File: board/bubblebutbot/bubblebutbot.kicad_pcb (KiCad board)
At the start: 2 copper layers, 80 x 86 mm, 15 parts, among them J1 Screw_Terminal_01x02, J2 Screw_Terminal_01x02, J3 Conn_01x06_Female, J4 Conn_01x06_Female, Q1 FDN336P, U1 WeMos_D1_mini, U2 18350-HOLDER, U3 TPS613222ADBV

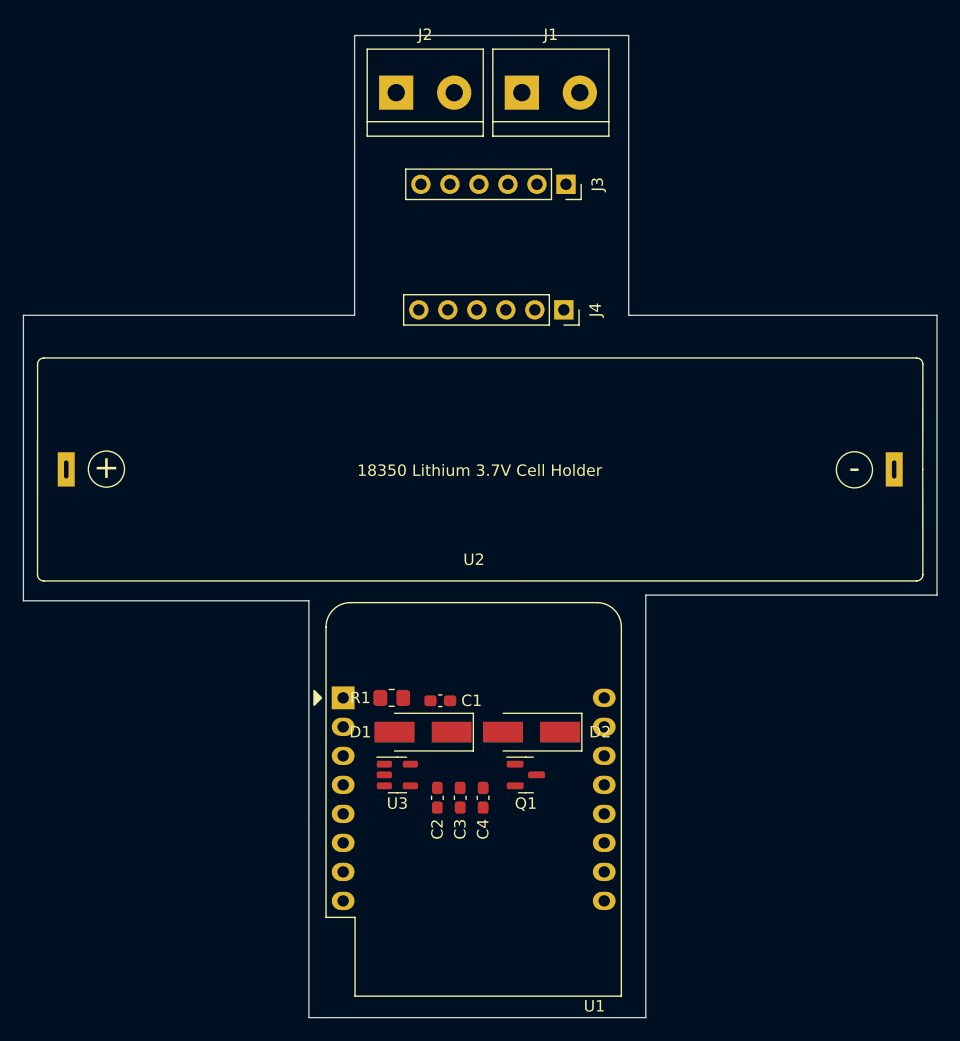
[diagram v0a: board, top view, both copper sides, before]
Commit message: Finished prototype pcb
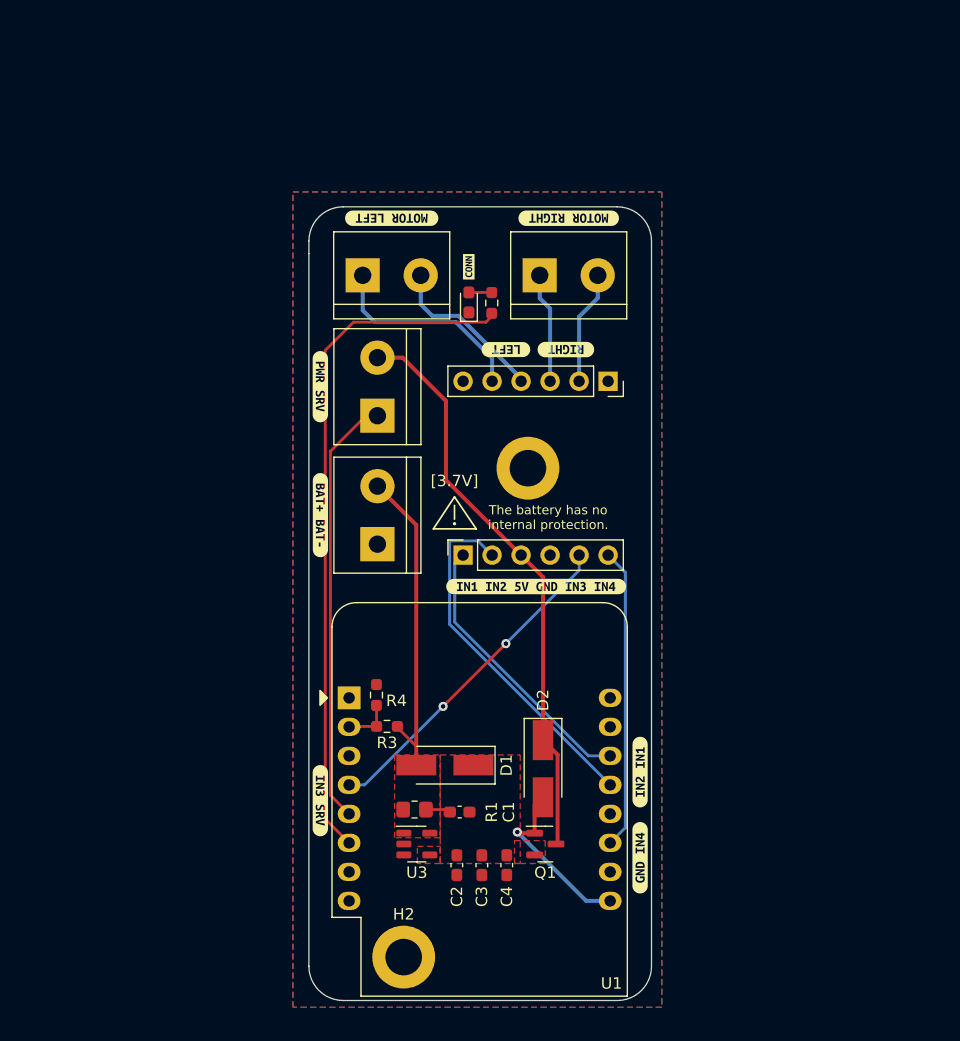
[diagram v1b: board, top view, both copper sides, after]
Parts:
- removed U2: 18350-HOLDER, CustomFootprints:18350-Holder
- added D3: LED, LED_SMD:LED_0603_1608Metric_Pad1.05x0.95mm_HandSolder, F.Cu at (165.0, 82.4)
- added H1: MountingHole, MountingHole:MountingHole_3.2mm_M3_ISO14580_Pad, F.Cu at (170.2, 96.9)
- added H2: MountingHole, MountingHole:MountingHole_3.2mm_M3_ISO14580_Pad, F.Cu at (159.3, 139.7)
- added J5: Screw_Terminal_01x02, TerminalBlock:TerminalBlock_bornier-2_P5.08mm, F.Cu at (157.0, 103.5)
- added J6: Screw_Terminal_01x02, TerminalBlock:TerminalBlock_bornier-2_P5.08mm, F.Cu at (157.0, 92.3)
- added R2: 1k, Resistor_SMD:R_0603_1608Metric_Pad0.98x0.95mm_HandSolder, F.Cu at (167.0, 82.4)
- added R3: 10k, Resistor_SMD:R_0603_1608Metric_Pad0.98x0.95mm_HandSolder, F.Cu at (157.8, 119.5)
- added R4: 33k, Resistor_SMD:R_0603_1608Metric_Pad0.98x0.95mm_HandSolder, F.Cu at (156.9, 116.8)
- added kibuzzard-641EE450: G***, kibuzzard-641EE450, F.Cu at (180.0, 123.5)
- added kibuzzard-641EE46F: G***, kibuzzard-641EE46F, F.Cu at (180.0, 131.0)
- added kibuzzard-641EE492: G***, kibuzzard-641EE492, F.Cu at (152.0, 126.0)
- added kibuzzard-641EE4C6: G***, kibuzzard-641EE4C6, F.Cu at (152.0, 101.0)
- added kibuzzard-641EE536: G***, kibuzzard-641EE536, F.Cu at (152.0, 89.8)
- added kibuzzard-641EE568: G***, kibuzzard-641EE568, F.Cu at (170.9, 107.2)
- added kibuzzard-641EE5F8: G***, kibuzzard-641EE5F8, F.Cu at (173.5, 86.5)
- added kibuzzard-641EE609: G***, kibuzzard-641EE609, F.Cu at (168.2, 86.5)
- added kibuzzard-641EE6B8: G***, kibuzzard-641EE6B8, F.Cu at (158.2, 75.0)
- added kibuzzard-641EE6C6: G***, kibuzzard-641EE6C6, F.Cu at (173.8, 75.0)
- added kibuzzard-641EE74D: G***, kibuzzard-641EE74D, F.Cu at (165.0, 79.2)
- moved J4 23.2 mm to (164.5, 104.5), turned to 90 degrees
- moved J3 17.6 mm to (177.2, 89.3)
- moved J2 16.3 mm to (155.7, 80.0)
- moved J1 16.1 mm to (171.2, 80.0)
- moved R1 9.98 mm to (160.2, 126.8)
- moved C1 9.90 mm to (164.2, 127.0)
- moved Q1 6.28 mm to (171.7, 129.8)
- moved U3 6.28 mm to (160.4, 129.8)
- moved C4 6.25 mm to (168.3, 131.7)
- moved C3 6.20 mm to (166.1, 131.7)
- moved C2 6.14 mm to (164.0, 131.7)
- moved D1 3.46 mm to (162.9, 122.9)
- moved D2 3.35 mm to (171.5, 123.2), turned to -90 degrees
- moved U1 0.52 mm to (154.5, 117.0)
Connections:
- U1 pad 2: unconnected-(U1-Pad2) -> BATTERY_LVL
- U1 pad 5: unconnected-(U1-Pad5) -> SERVO_PWM
- U1 pad 6: unconnected-(U1-Pad6) -> Net-(U1-Pad6)
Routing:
- net Net-(U1-Pad6): track 0.00 -> 60.2 mm
- net SPLY: track 0.00 -> 50.5 mm
- net SERVO_PWM: track 0.00 -> 37.8 mm
- net IN2: track 0.00 -> 31.4 mm
- net Net-(D1-Pad2): track 0.00 -> 30.0 mm
- net IN3: track 0.00 -> 29.3 mm, vias 0 -> 2
- net IN4: track 0.00 -> 26.4 mm
- net IN1: track 0.00 -> 24.6 mm
- net Net-(J2-Pad1): track 0.00 -> 17.9 mm
- net WEMOS_USB_POWER: track 0.00 -> 15.6 mm, vias 0 -> 1
- net Net-(J2-Pad2): track 0.00 -> 14.3 mm
- net Net-(J1-Pad2): track 0.00 -> 9.70 mm
- net Net-(J1-Pad1): track 0.00 -> 9.40 mm
- net BATTERY_LVL: track 0.00 -> 4.12 mm
- net Net-(C1-Pad1): track 0.00 -> 2.18 mm
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- added copper zone on B.Cu, net GND
- added copper zone on F.Cu, net GND
- added copper zone on F.Cu, net Net-(C1-Pad2)
- added copper zone on F.Cu, net Net-(D1-Pad2)
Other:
- board size 80 x 86 mm -> 30 x 69.5 mm
- board text added: "The battery has no internal protection."
- board text added: "[3.7V]"

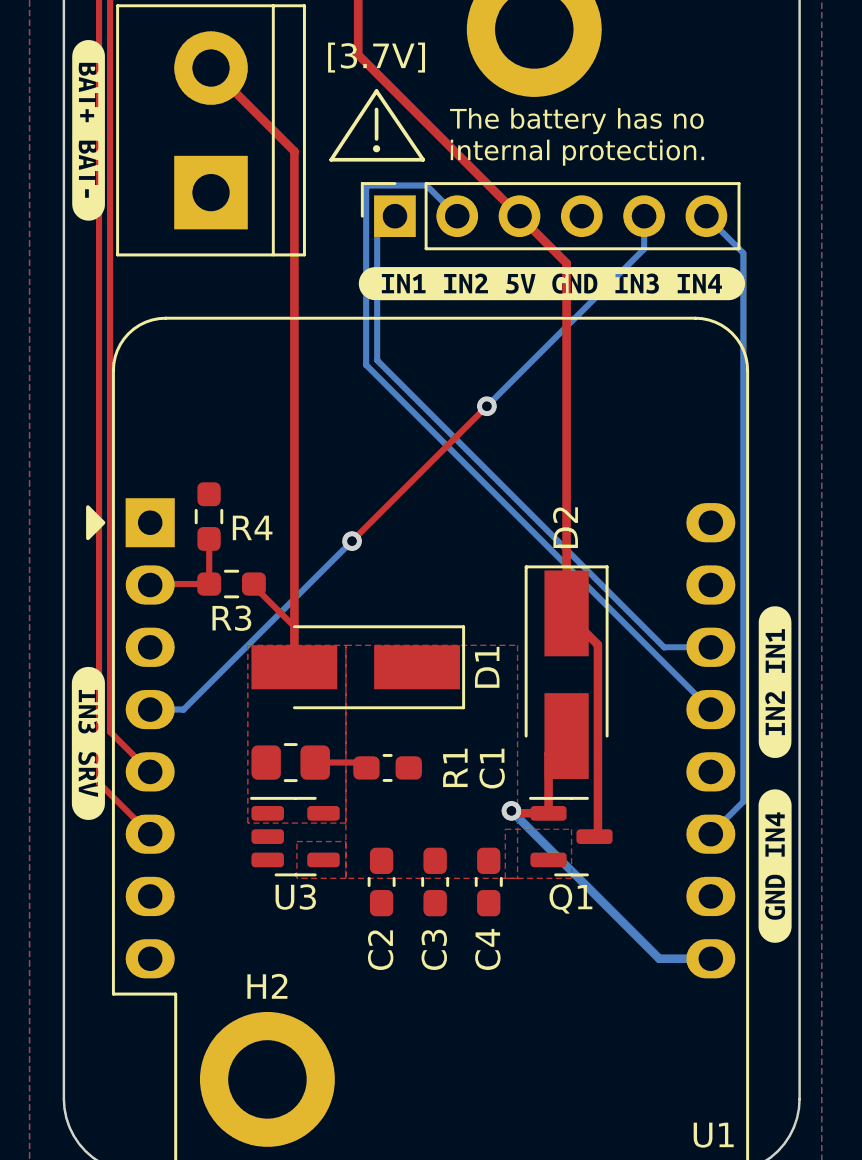
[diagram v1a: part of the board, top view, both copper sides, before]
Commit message: Added a missing inductor to the design
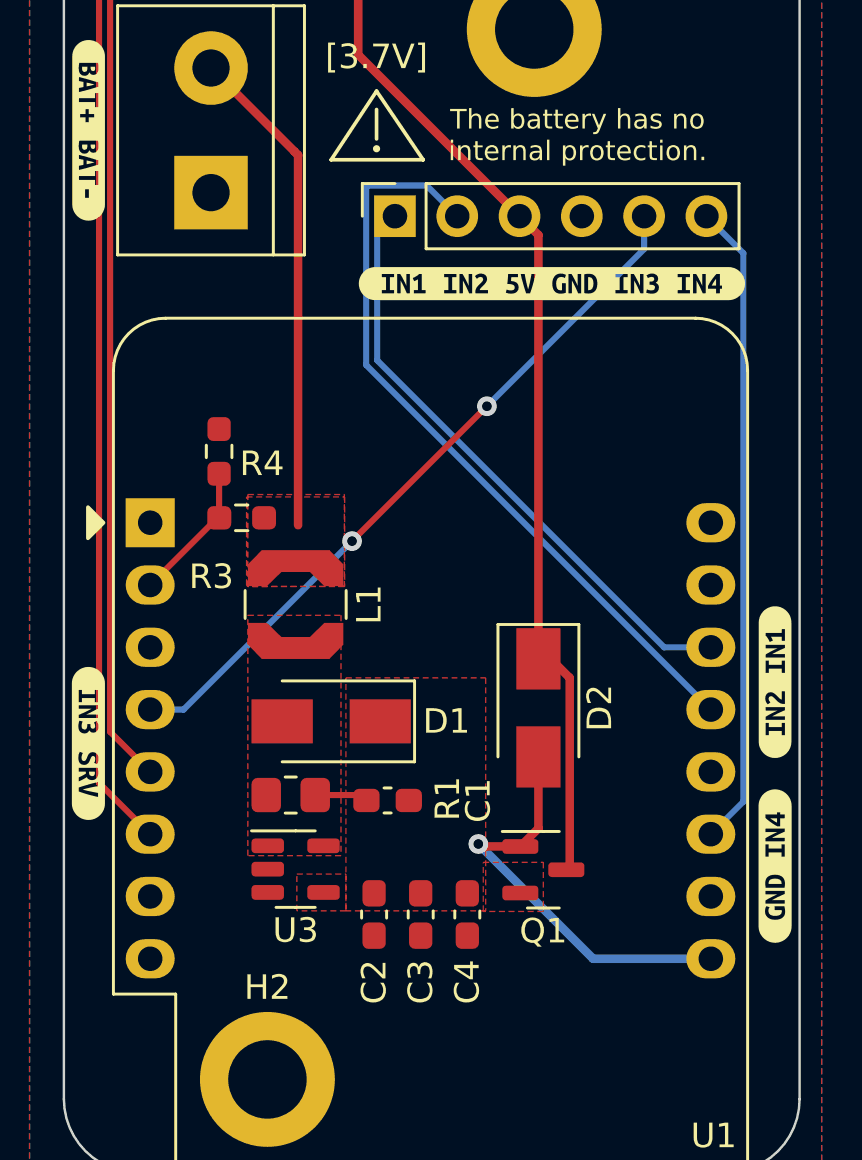
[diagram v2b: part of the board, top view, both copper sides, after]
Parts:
- added L1: 2.2u, Inductor_SMD:L_Coilcraft_LPS4018, F.Cu at (160.4, 120.3)
- D1, D2: footprint Diode_SMD:D_SMA_Handsoldering -> Diode_SMD:D_SMA
- moved R3 2.73 mm to (158.2, 116.8)
- moved R4 2.69 mm to (157.3, 114.1)
- moved D1 2.42 mm to (161.9, 125.1)
- moved D2 1.77 mm to (170.3, 124.5)
- moved Q1 1.77 mm to (170.6, 131.2)
- moved C4 1.59 mm to (167.4, 133.0)
- moved C3 1.45 mm to (165.6, 133.0)
- moved C2 1.36 mm to (163.7, 133.0)
- moved C1 1.32 mm to (164.2, 128.3)
- moved R1 1.32 mm to (160.2, 128.1)
- moved U3 1.32 mm to (160.4, 131.1)
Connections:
- J5 pad 2: Net-(D1-Pad2) -> Net-(J5-Pad2)
- R3 pad 1: Net-(D1-Pad2) -> Net-(J5-Pad2)
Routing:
- net Net-(D1-Pad2): track 30.0 -> 0.00 mm
- net Net-(J5-Pad2): track 0.00 -> 20.1 mm
- net BATTERY_LVL: track 4.12 -> 5.75 mm
- net WEMOS_USB_POWER: track 15.6 -> 16.9 mm
- net SPLY: track 50.5 -> 51.3 mm
- added copper zone on F.Cu, net Net-(J5-Pad2)

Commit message: gerber for 1v01 ready
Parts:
- removed J5, J6: Screw_Terminal_01x02, TerminalBlock:TerminalBlock_bornier-2_P5.08mm
- J1, J2: value Screw_Terminal_01x02 -> Screw_Terminal_01x04; footprint TerminalBlock:TerminalBlock_bornier-2_P5.08mm -> TerminalBlock_MetzConnect:TerminalBlock_MetzConnect_Type094_RT03504HBLU_1x04_P5.00mm_Horizontal
- moved J1 26.9 mm to (157.8, 103.3), turned to 90 degrees
- moved D3 11.3 mm to (153.8, 81.0)
- moved R2 11.3 mm to (155.8, 81.0)
- moved kibuzzard-641EE74D 11.3 mm to (153.8, 77.8)
- moved J2 5.42 mm to (161.1, 80.6)
- moved kibuzzard-641EE6B8 5.35 mm to (163.6, 75.0)
- moved kibuzzard-641EE536 1.05 mm to (152.0, 90.8)
- moved kibuzzard-641EE4C6 0.20 mm to (152.0, 100.8)
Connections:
- J1 pad 1: Net-(J1-Pad1) -> GND
- J1 pad 2: Net-(J1-Pad2) -> Net-(L1-Pad1)
- J3 pad 2: Net-(J1-Pad2) -> Net-(J3-Pad2)
- J3 pad 3: Net-(J1-Pad1) -> Net-(J3-Pad3)
- L1 pad 1: Net-(J5-Pad2) -> Net-(L1-Pad1)
- R3 pad 1: Net-(J5-Pad2) -> Net-(L1-Pad1)
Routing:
- net Net-(J5-Pad2): track 20.1 -> 0.00 mm
- net Net-(L1-Pad1): track 0.00 -> 19.9 mm
- net Net-(R2-Pad1): track 60.2 -> 50.1 mm
- net Net-(J1-Pad2): track 9.70 -> 0.00 mm
- net Net-(J1-Pad1): track 9.40 -> 0.00 mm
- net Net-(J3-Pad2): track 0.00 -> 9.32 mm
- net Net-(J3-Pad3): track 0.00 -> 9.14 mm
- net Net-(J3-Pad5): track 17.9 -> 11.2 mm
- net Net-(J3-Pad4): track 14.3 -> 10.2 mm
- net SPLY: track 51.3 -> 50.1 mm
- added copper zone on F.Cu, net Net-(L1-Pad1)
- removed copper zone on F.Cu, net Net-(J5-Pad2)
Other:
- board size 30 x 69.5 mm -> 30 x 70 mm
- board text added: "1v01"
